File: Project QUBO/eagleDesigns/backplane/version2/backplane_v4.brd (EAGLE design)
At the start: 102 x 152 mm, 288 parts, among them U1 TUSB2077ALQFP

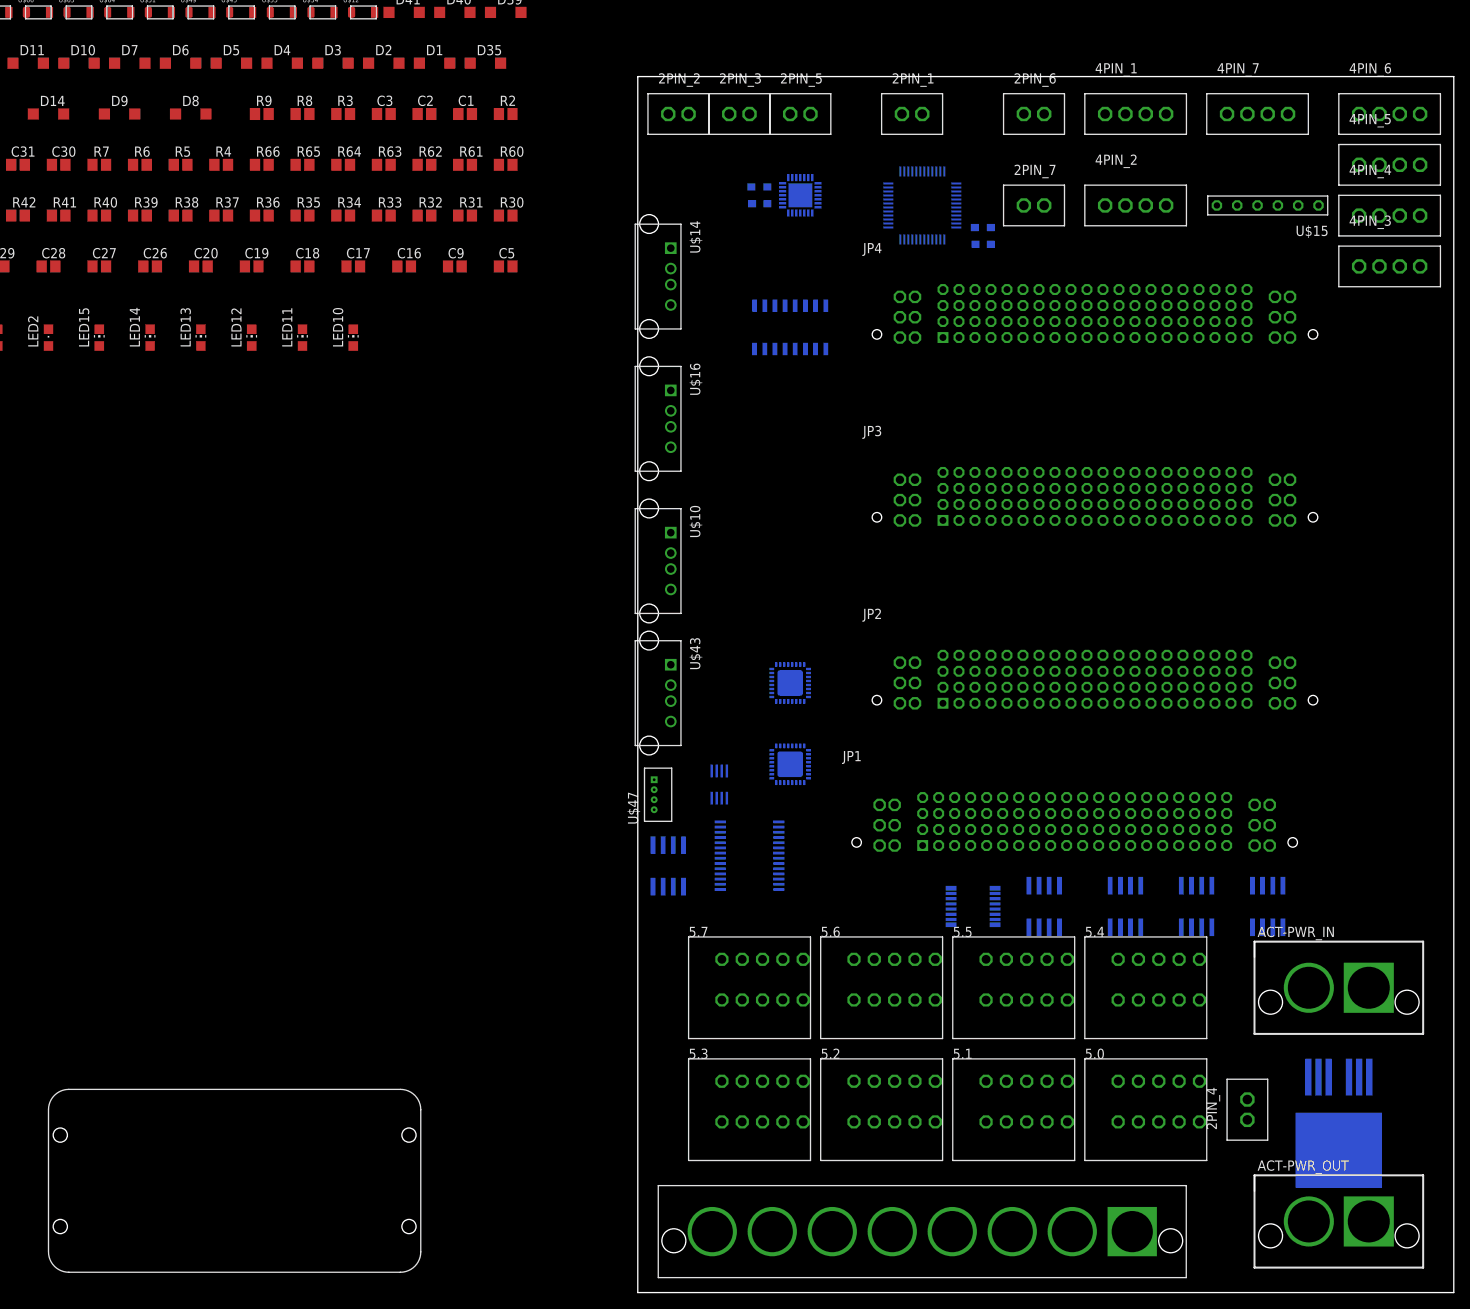
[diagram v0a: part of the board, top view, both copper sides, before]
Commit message: 
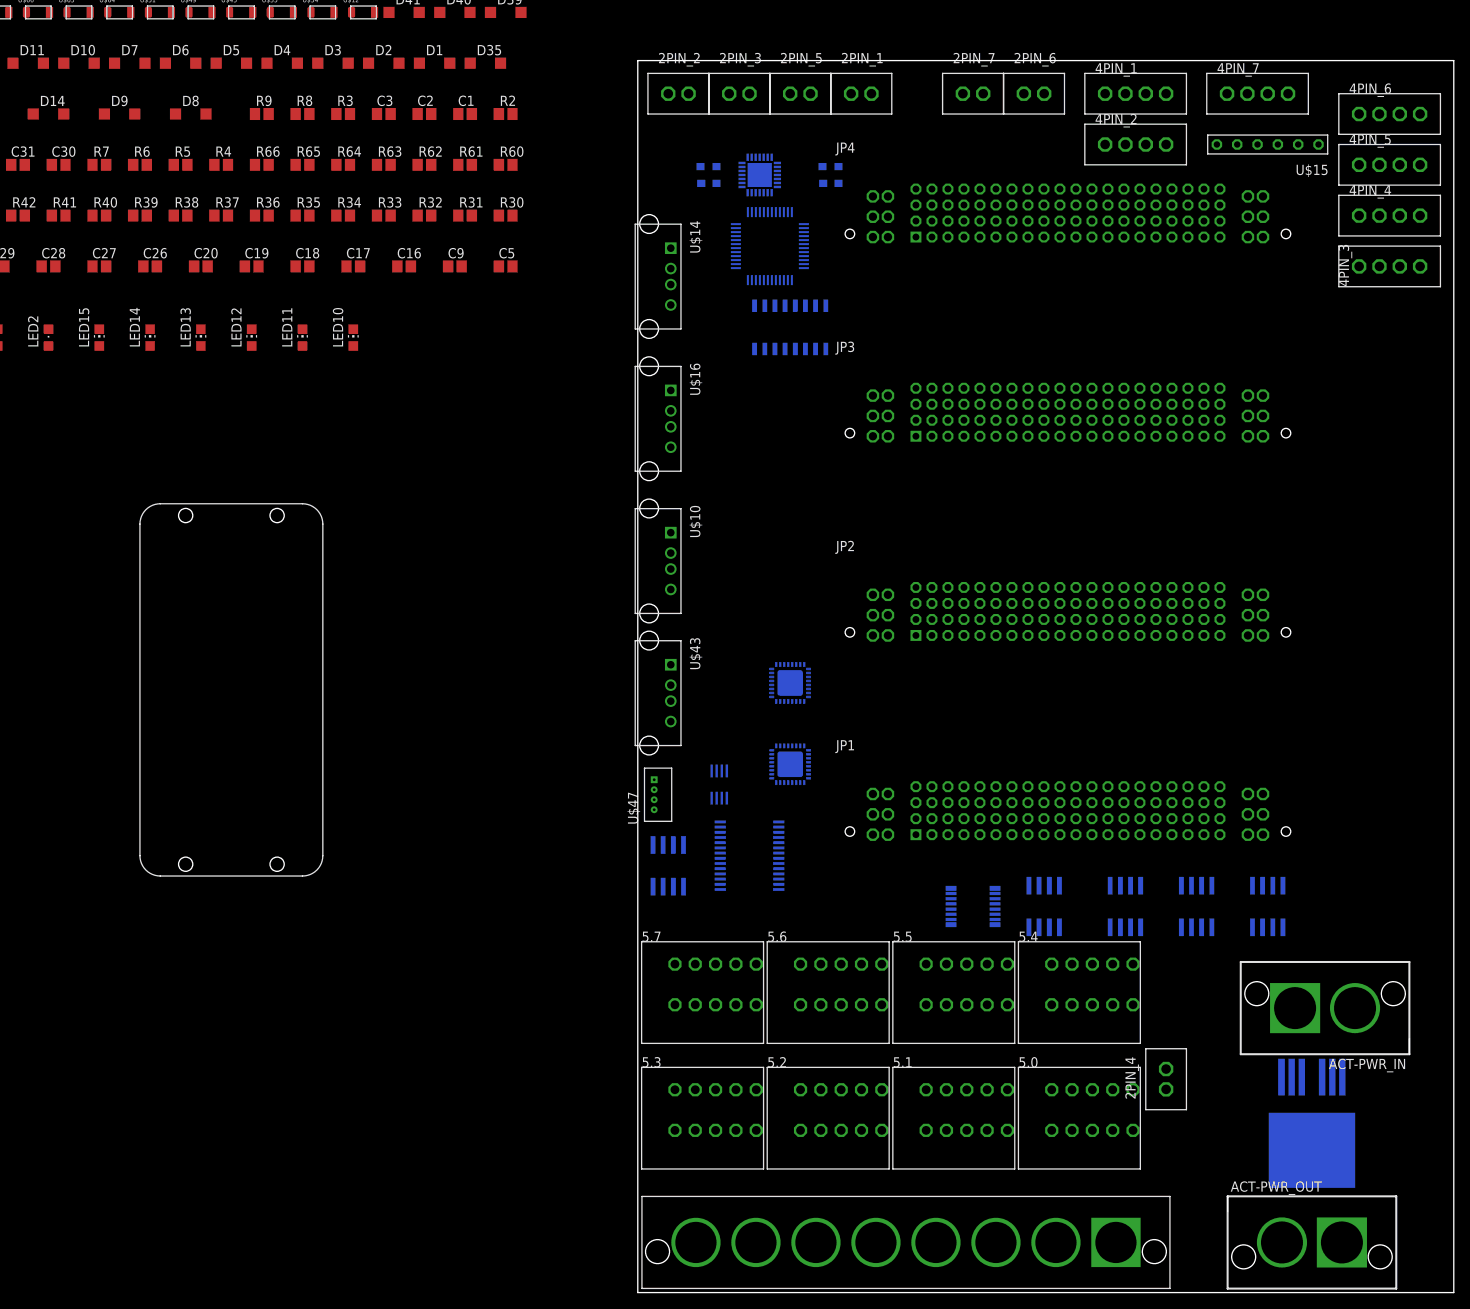
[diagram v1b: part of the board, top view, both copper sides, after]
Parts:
- moved U$13 60.2 mm to (-39.4, 52.1), turned to 90 degrees
- moved U$33 20.5 mm to (24.1, 139.7)
- moved U1 19.7 mm to (16.5, 130.8)
- moved 2PIN_7 15.9 mm to (41.9, 149.9)
- moved JP4 13.0 mm to (53.8, 134.5)
- moved JP3 11.0 mm to (53.8, 109.6)
- moved 2PIN_4 10.9 mm to (66.0, 26.7)
- moved JP2 9.13 mm to (53.8, 84.7)
- moved 5.0 8.37 mm to (55.2, 21.8)
- moved 5.4 8.32 mm to (55.2, 37.5)
- moved 4PIN_2 7.62 mm to (62.2, 143.5)
- moved U$15 7.62 mm to (78.7, 143.5)
- moved 5.1 7.56 mm to (39.5, 21.8)
- moved 5.5 7.51 mm to (39.5, 37.5)
- moved 2PIN_1 6.84 mm to (27.9, 149.9)
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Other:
- board size 102 x 152 mm -> 102 x 154 mm

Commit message: 
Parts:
- moved 5.4 35.1 mm to (23.8, 21.8)
- moved 5.3 35.1 mm to (39.5, 37.5)
- moved 5.1 22.2 mm to (55.2, 37.5)
- moved 5.6 22.2 mm to (8.10, 21.8)
- moved 5.2 15.7 mm to (39.5, 21.8)
- moved 5.5 15.7 mm to (23.8, 37.5)
- moved U$100 6.35 mm to (39.9, 6.26)
- moved ACT-PWR_OUT 5.08 mm to (84.3, 11.3)
- moved ACT-PWR_IN 4.02 mm to (84.6, 39.4)
- moved U$41 3.81 mm to (84.3, 21.6)
- moved 2PIN_3 2.54 mm to (15.2, 149.9)
- moved 2PIN_2 2.54 mm to (7.62, 149.9)
- moved 2PIN_1 2.54 mm to (30.5, 149.9)
- moved 2PIN_5 2.54 mm to (22.9, 149.9)
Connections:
- net 5V: now also U$10.VDD, U$43.VDD; no longer U$10.1, U$43.1
- net AHRS_USB_M: now also U$43.D+; no longer U$43.3
- net AHRS_USB_P: now also U$43.D-; no longer U$43.2
- net GND: now also U$10.GND, U$14.GND, U$16.GND, U$43.GND; no longer U$10.4, U$14.4, U$16.4, U$43.4
- net IMU_USB_M: now also U$10.D+; no longer U$10.3
- net IMU_USB_P: now also U$10.D-; no longer U$10.2
- net USB_5_5V: now also U$14.VDD; no longer U$14.1
- net USB_5_M: now also U$14.D+; no longer U$14.3
- net USB_5_P: now also U$14.D-; no longer U$14.2
- net USB_6_5V: now also U$16.VDD; no longer U$16.1
- net USB_6_M: now also U$16.D+; no longer U$16.3
- net USB_6_P: now also U$16.D-; no longer U$16.2

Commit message: 
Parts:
- added U$101, U$102, U$103, U$104, U$105, U$106, U$107, U$108, U$109, U$17, U$21, U$26, U$36, U$74: (no value), resistor:R0805
- moved U$14 1.27 mm to (2.54, 128.3)
- moved U$10 1.27 mm to (2.54, 92.7)
- moved U$16 1.27 mm to (2.54, 110.5)
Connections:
- removed net GND1: D37.A, U$11.P$1, U$12.P$2
- removed net GND2: D36.A, U$44.P$1, U$45.P$2
- removed net GND3: D10.A, U$48.P$1, U$49.P$2
- removed net USB_5_5V1: D37.C, U$11.P$2, U$12.P$1
- removed net USB_5_5V2: D36.C, U$44.P$2, U$45.P$1
- removed net USB_5_5V3: D10.C, U$48.P$2, U$49.P$1
- new net N$27: U$10.VDD, U$17.2
- new net N$28: U$10.GND, U$21.2
- new net N$29: U$10.SHIELD, U$10.SHIELD1, U$26.2
- new net N$30: U$108.2, U$47.P$1
- new net N$37: U$109.2, U$47.P$4
- new net N$38: U$43.VDD, U$74.2
- new net N$40: U$101.2, U$43.GND
- new net N$41: U$36.2, U$43.SHIELD, U$43.SHIELD1
- new net N$42: U$107.2, U$14.VDD
- new net N$73: U$106.2, U$14.GND
- new net N$80: U$105.2, U$14.SHIELD, U$14.SHIELD1
- new net N$83: U$104.2, U$16.SHIELD, U$16.SHIELD1
- new net N$84: U$102.2, U$16.VDD
- new net N$85: U$103.2, U$16.GND
- net 5V: now also D10.C, D36.C, D37.C, U$108.1, U$11.P$2, U$12.P$1, U$17.1, U$44.P$2, U$45.P$1, U$48.P$2, U$49.P$1, U$74.1; no longer U$10.VDD, U$43.VDD, U$47.P$1
- net GND: now also D10.A, D36.A, D37.A, U$101.1, U$103.1, U$104.1, U$105.1, U$106.1, U$109.1, U$11.P$1, U$12.P$2, U$21.1, U$26.1, U$36.1, U$44.P$1, U$45.P$2, U$48.P$1, U$49.P$2; no longer U$10.GND, U$14.GND, U$16.GND, U$43.GND, U$47.P$4
- net USB_5_5V: now also U$107.1; no longer U$14.VDD
- net USB_6_5V: now also U$102.1; no longer U$16.VDD

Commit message: 
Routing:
- added copper zone on layer 16, net ACT-PWR_POST-KILL
- added copper zone on layer 16, net ACT-PWR_PRE-KILL

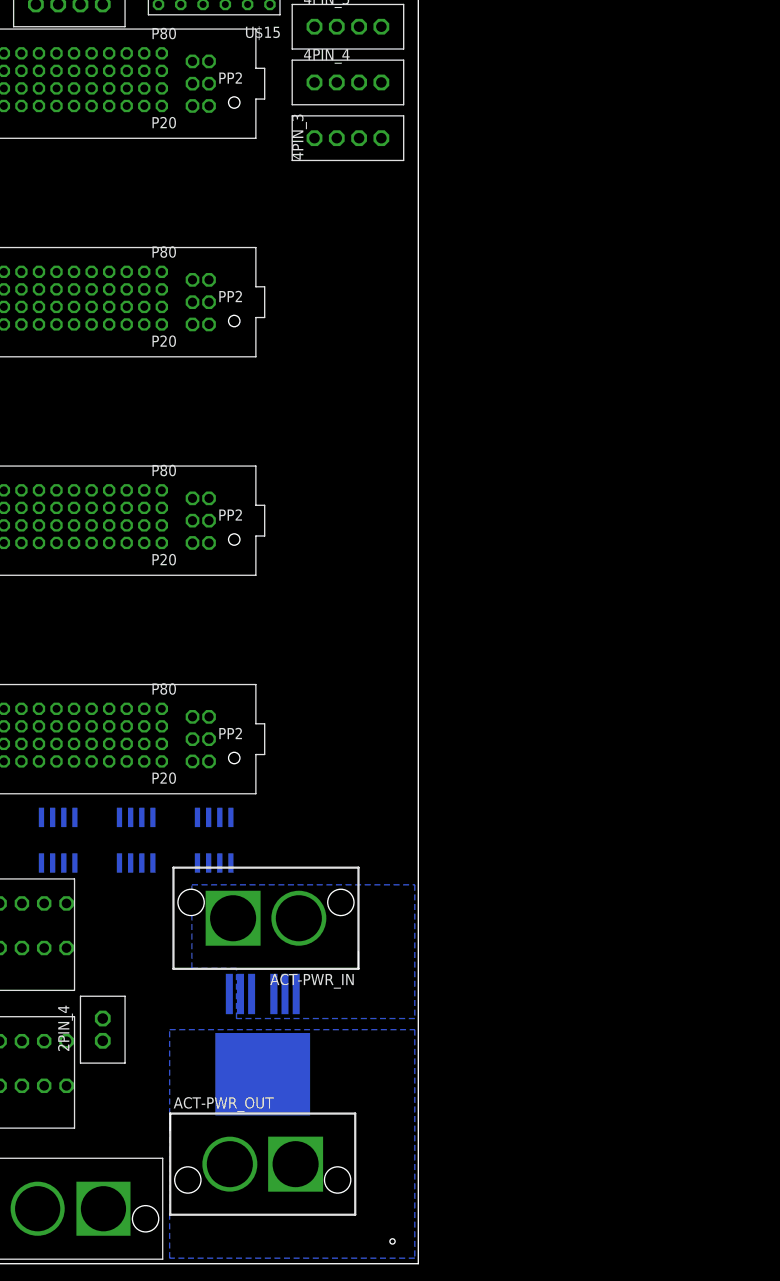
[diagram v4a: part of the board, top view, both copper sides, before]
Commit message: 
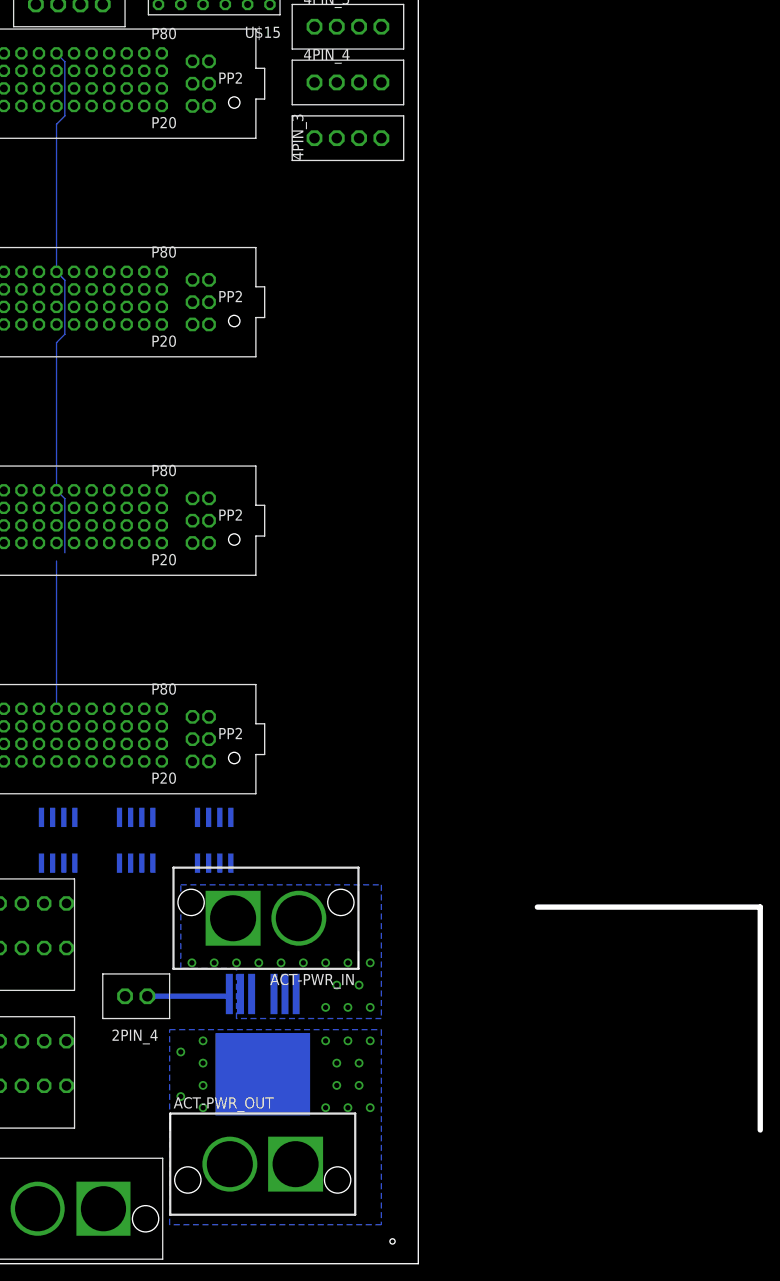
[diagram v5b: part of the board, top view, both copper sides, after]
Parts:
- moved 2PIN_4 5.39 mm to (69.8, 30.5), turned to 180 degrees
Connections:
- net RTS_0 renamed RX_SF
- net SCL_0_UNBUF renamed BATT_SCL_UNBUF
- net SDA_0_UNBUF renamed BATT_SDA_UNBUF
- removed net CTS_0: JP1.47, JP2.47, JP3.47, JP4.47
- removed net CTS_1: JP1.31, JP2.31, JP3.31, JP4.31
- removed net CTS_2: 4PIN_1.P$1, JP1.71, JP2.71, JP3.71, JP4.71
- removed net CTS_3: 4PIN_2.P$1, JP1.75, JP2.75, JP3.75, JP4.75
- removed net CTS_4: JP1.79, JP2.79, JP3.79, JP4.79
- removed net CTS_5: 5.2.P$5, 5.2.P$6, JP1.67, JP2.67, JP3.67, JP4.67, U$55.P$3
- removed net GND\: DVL_USB_HUB.P$29, JP1.40, JP2.40, JP3.40, JP4.40
- removed net GPIO_0: JP1.35, JP2.35, JP3.35, JP4.35
- removed net GPIO_1: JP1.38, JP2.38, JP3.38, JP4.38
- removed net GPIO_3: JP1.57, JP2.57, JP3.57, JP4.57
- removed net GPIO_4: JP1.58, JP2.58, JP3.58, JP4.58
- removed net NC: JP1.13, JP1.14, JP1.16, JP1.17, JP2.13, JP2.14, JP2.16, JP2.17, JP3.13, JP3.14, JP3.16, JP3.17, JP4.13, JP4.14, JP4.16, JP4.17
- removed net RTS_1: JP1.32, JP2.32, JP3.32, JP4.32
- removed net RTS_2: 4PIN_1.P$2, JP1.72, JP2.72, JP3.72, JP4.72
- removed net RTS_3: 4PIN_2.P$2, JP1.76, JP2.76, JP3.76, JP4.76
- removed net RTS_4: JP1.80, JP2.80, JP3.80, JP4.80
- removed net RTS_5: 5.2.P$7, 5.2.P$8, JP1.68, JP2.68, JP3.68, JP4.68, U$55.P$2
- removed net RX_0: JP1.45, JP2.45, JP3.45, JP4.45
- removed net RX_1: JP1.29, JP2.29, JP3.29, JP4.29
- removed net RX_2: 4PIN_1.P$4, JP1.69, JP2.69, JP3.69, JP4.69, U$4.P$3
- removed net RX_3: 4PIN_2.P$4, JP1.73, JP2.73, JP3.73, JP4.73, U$8.P$2
- removed net RX_4: JP1.77, JP2.77, JP3.77, JP4.77
- removed net RX_5: 5.2.P$1, 5.2.P$2, JP1.65, JP2.65, JP3.65, JP4.65, U$54.P$2
- removed net SCL_0: JP1.28, JP2.28, JP3.28, JP4.28, U$38.2
- removed net SCL_1: 2PIN_6.P$1, JP1.10, JP2.10, JP3.10, JP4.10, U$18.P$2, U$50.2
- removed net SCL_2: 5.4.P$10, 5.4.P$9, JP1.60, JP2.60, JP3.60, JP4.60, U$63.P$2
- removed net SCL_3: 5.3.P$3, 5.3.P$4, JP1.6, JP2.6, JP3.6, JP4.6, U$52.P$2
- removed net SDA_0: JP1.27, JP2.27, JP3.27, JP4.27, U$38.7
- removed net SDA_1: 2PIN_6.P$2, JP1.9, JP2.9, JP3.9, JP4.9, U$18.P$3, U$50.7
- removed net SDA_2: 5.5.P$10, 5.5.P$9, JP1.59, JP2.59, JP3.59, JP4.59, U$63.P$3
- removed net SDA_3: 5.3.P$1, 5.3.P$2, JP1.5, JP2.5, JP3.5, JP4.5, U$52.P$3
- removed net TX_0: JP1.46, JP2.46, JP3.46, JP4.46
- removed net TX_1: JP1.30, JP2.30, JP3.30, JP4.30
- removed net TX_2: 4PIN_1.P$3, JP1.70, JP2.70, JP3.70, JP4.70, U$4.P$2
- removed net TX_3: 4PIN_2.P$3, JP1.74, JP2.74, JP3.74, JP4.74, U$8.P$3
- removed net TX_4: JP1.78, JP2.78, JP3.78, JP4.78
- removed net TX_5: 5.2.P$3, 5.2.P$4, JP1.66, JP2.66, JP3.66, JP4.66, U$54.P$3
- removed net USB_1_M: JP1.19, R2.1, R22.1, U$29.P$3
- removed net USB_2_M: JP2.19, R24.1, R37.1, U$30.P$3
- removed net USB_3_M: JP3.19, R27.2, R40.1, U$31.P$3
- removed net USB_4_M: JP4.19, R28.2, R41.1, U$32.P$3
- new net ACT_SCL: 5.4.P$10, 5.4.P$9, JP1.24, JP2.24, JP3.24, JP4.24, U$63.P$2
- new net ACT_SDA: 5.5.P$10, 5.5.P$9, JP1.23, JP2.23, JP3.23, JP4.23, U$63.P$3
- new net BATT_SCL: JP1.44, JP2.44, JP3.44, JP4.44, U$38.2
- new net BATT_SDA: JP1.43, JP2.43, JP3.43, JP4.43, U$38.7
- new net CTS_CF: 4PIN_2.P$1, JP1.13, JP2.13, JP3.13, JP4.13
- new net CTS_MC: 4PIN_1.P$1, JP1.29, JP2.29, JP3.29, JP4.29
- new net CTS_MD: 5.2.P$5, 5.2.P$6, JP1.68, JP2.68, JP3.68, JP4.68, U$55.P$3
- new net CTS_MF: JP1.5, JP2.5, JP3.5, JP4.5
- new net CTS_PF: JP1.9, JP2.9, JP3.9, JP4.9
- new net CTS_SF: JP1.50, JP2.50, JP3.50, JP4.50
- new net EXT_SCL: 5.3.P$3, 5.3.P$4, JP1.34, JP2.34, JP3.34, JP4.34, U$52.P$2
- new net EXT_SDA: 5.3.P$1, 5.3.P$2, JP1.33, JP2.33, JP3.33, JP4.33, U$52.P$3
- new net GPIO_22: JP1.22, JP2.22, JP3.22, JP4.22
- new net GPIO_63: JP1.63, JP2.63, JP3.63, JP4.63
- new net INT_SCL: 2PIN_6.P$1, JP1.65, JP2.65, JP3.65, JP4.65, U$18.P$2, U$50.2
- new net INT_SDA: 2PIN_6.P$2, JP1.64, JP2.64, JP3.64, JP4.64, U$18.P$3, U$50.7
- new net RTS_CF: 4PIN_2.P$2, JP1.14, JP2.14, JP3.14, JP4.14
- new net RTS_MC: 4PIN_1.P$2, JP1.30, JP2.30, JP3.30, JP4.30
- new net RTS_MD: 5.2.P$7, 5.2.P$8, JP1.69, JP2.69, JP3.69, JP4.69, U$55.P$2
- new net RTS_MF: JP1.6, JP2.6, JP3.6, JP4.6
- new net RTS_PF: JP1.10, JP2.10, JP3.10, JP4.10
- new net RTS_SF: JP1.51, JP2.51, JP3.51, JP4.51
- new net RX_CF: 4PIN_2.P$4, JP1.11, JP2.11, JP3.11, JP4.11, U$8.P$2
- new net RX_MC: 4PIN_1.P$4, JP1.27, JP2.27, JP3.27, JP4.27, U$4.P$3
- new net RX_MD: 5.2.P$1, 5.2.P$2, JP1.66, JP2.66, JP3.66, JP4.66, U$54.P$2
- new net RX_MF: JP1.3, JP2.3, JP3.3, JP4.3
- new net RX_PF: JP1.7, JP2.7, JP3.7, JP4.7
- new net TX_CF: 4PIN_2.P$3, JP1.12, JP2.12, JP3.12, JP4.12, U$8.P$3
- new net TX_MC: 4PIN_1.P$3, JP1.28, JP2.28, JP3.28, JP4.28, U$4.P$2
- new net TX_MD: 5.2.P$3, 5.2.P$4, JP1.67, JP2.67, JP3.67, JP4.67, U$54.P$3
- new net TX_MF: JP1.4, JP2.4, JP3.4, JP4.4
- new net TX_PF: JP1.8, JP2.8, JP3.8, JP4.8
- new net TX_SF: JP1.49, JP2.49, JP3.49, JP4.49
- new net USB_1_N: JP1.61, R2.1, R22.1, U$29.P$3
- new net USB_2_N: JP2.61, R24.1, R37.1, U$30.P$3
- new net USB_3_N: JP3.61, R27.2, R40.1, U$31.P$3
- new net USB_4_N: JP4.61, R28.2, R41.1, U$32.P$3
- net 12V: now also JP1.16, JP1.36, JP1.56, JP1.76, JP2.16, JP2.36, JP2.56, JP2.76, JP3.16, JP3.36, JP3.56, JP3.76, JP4.16, JP4.36, JP4.56, JP4.76; no longer JP1.1, JP1.21, JP1.41, JP1.61, JP2.1, JP2.21, JP2.41, JP2.61, JP3.1, JP3.21, JP3.41, JP3.61, JP4.1, JP4.21, JP4.41, JP4.61
- net 3V3: now also JP1.18, JP1.38, JP1.58, JP1.78, JP2.18, JP2.38, JP2.58, JP2.78, JP3.18, JP3.38, JP3.58, JP3.78, JP4.18, JP4.38, JP4.58, JP4.78; no longer JP1.23, JP1.3, JP1.43, JP1.63, JP2.23, JP2.3, JP2.43, JP2.63, JP3.23, JP3.3, JP3.43, JP3.63, JP4.23, JP4.3, JP4.43, JP4.63
- net 5V: now also JP1.17, JP1.37, JP1.57, JP1.77, JP2.17, JP2.37, JP2.57, JP2.77, JP3.17, JP3.37, JP3.57, JP3.77, JP4.17, JP4.37, JP4.57, JP4.77; no longer JP1.2, JP1.22, JP1.42, JP1.62, JP2.2, JP2.22, JP2.42, JP2.62, JP3.2, JP3.22, JP3.42, JP3.62, JP4.2, JP4.22, JP4.42, JP4.62
- net CANH: now also JP1.45, JP2.45, JP3.45, JP4.45; no longer JP1.25, JP2.25, JP3.25, JP4.25
- net CANL: now also JP1.46, JP2.46, JP3.46, JP4.46; no longer JP1.26, JP2.26, JP3.26, JP4.26
- net CE_2: now also JP1.52, JP2.52, JP3.52, JP4.52; no longer JP1.54, JP2.54, JP3.54, JP4.54
- net CE_3: now also JP1.53, JP2.53, JP3.53, JP4.53; no longer JP1.55, JP2.55, JP3.55, JP4.55
- net CE_4: now also JP1.54, JP2.54, JP3.54, JP4.54; no longer JP1.56, JP2.56, JP3.56, JP4.56
- net CE_CPU: now also JP1.74, JP2.74, JP3.74, JP4.74; no longer JP1.53, JP2.53, JP3.53, JP4.53
- net CE_LEDS: now also JP1.73, JP2.73, JP3.73, JP4.73; no longer JP1.52, JP2.52, JP3.52, JP4.52
- net GND: now also DVL_USB_HUB.P$29, JP1.1, JP1.19, JP1.20, JP1.21, JP1.25, JP1.32, JP1.35, JP1.40, JP1.42, JP1.47, JP1.55, JP1.59, JP1.60, JP1.62, JP1.75, JP1.79, JP1.80, JP1.P1,1, JP1.P1,2, JP1.P1,3, JP1.P1,4, JP1.P1,5, JP1.P1,6, JP2.1, JP2.19, JP2.20, JP2.21, JP2.25, JP2.32, JP2.35, JP2.40, JP2.42, JP2.47, JP2.55, JP2.59, JP2.60, JP2.62, JP2.75, JP2.79, JP2.80, JP2.P1,1, JP2.P1,2, JP2.P1,3, JP2.P1,4, JP2.P1,5, JP2.P1,6, JP3.1, JP3.19, JP3.20, JP3.21, JP3.25, JP3.32, JP3.35, JP3.40, JP3.42, JP3.47, JP3.55, JP3.59, JP3.60, JP3.62, JP3.75, JP3.79, JP3.80, JP3.P1,1, JP3.P1,2, JP3.P1,3, JP3.P1,4, JP3.P1,5, JP3.P1,6, JP4.1, JP4.19, JP4.20, JP4.21, JP4.25, JP4.32, JP4.35, JP4.40, JP4.42, JP4.47, JP4.55, JP4.59, JP4.60, JP4.62, JP4.75, JP4.79, JP4.80, JP4.P1,1, JP4.P1,2, JP4.P1,3, JP4.P1,4, JP4.P1,5, JP4.P1,6; no longer JP1.12, JP1.18, JP1.24, JP1.33, JP1.34, JP1.36, JP1.37, JP1.4, JP1.44, JP1.64, JP1.P2,1, JP1.P2,2, JP1.P2,3, JP1.P2,4, JP1.P2,5, JP1.P2,6, JP2.12, JP2.18, JP2.24, JP2.33, JP2.34, JP2.36, JP2.37, JP2.4, JP2.44, JP2.64, JP2.P2,1, JP2.P2,2, JP2.P2,3, JP2.P2,4, JP2.P2,5, JP2.P2,6, JP3.12, JP3.18, JP3.24, JP3.33, JP3.34, JP3.36, JP3.37, JP3.4, JP3.44, JP3.64, JP3.P2,1, JP3.P2,2, JP3.P2,3, JP3.P2,4, JP3.P2,5, JP3.P2,6, JP4.12, JP4.18, JP4.24, JP4.33, JP4.34, JP4.36, JP4.37, JP4.4, JP4.44, JP4.64, JP4.P2,1, JP4.P2,2, JP4.P2,3, JP4.P2,4, JP4.P2,5, JP4.P2,6
- net GPIO_2: now also JP1.2, JP2.2, JP3.2, JP4.2; no longer JP1.11, JP2.11, JP3.11, JP4.11
- net MISO: now also JP1.72, JP2.72, JP3.72, JP4.72; no longer JP1.51, JP2.51, JP3.51, JP4.51
- net MOSI: now also JP1.71, JP2.71, JP3.71, JP4.71; no longer JP1.50, JP2.50, JP3.50, JP4.50
- net PWM_0: now also JP1.31, JP2.31, JP3.31, JP4.31; no longer JP1.7, JP2.7, JP3.7, JP4.7
- net PWM_1: now also JP1.26, JP2.26, JP3.26, JP4.26; no longer JP1.8, JP2.8, JP3.8, JP4.8
- net SPI_CLK: now also JP1.70, JP2.70, JP3.70, JP4.70; no longer JP1.49, JP2.49, JP3.49, JP4.49
- net USB_1_P: now also JP1.41; no longer JP1.20
- net USB_2_P: now also JP2.41; no longer JP2.20
- net USB_3_P: now also JP3.41; no longer JP3.20
- net USB_4_P: now also JP4.41; no longer JP4.20
- net V_BATT: now also JP1.P2,1, JP1.P2,2, JP1.P2,3, JP1.P2,4, JP1.P2,5, JP1.P2,6, JP2.P2,1, JP2.P2,2, JP2.P2,3, JP2.P2,4, JP2.P2,5, JP2.P2,6, JP3.P2,1, JP3.P2,2, JP3.P2,3, JP3.P2,4, JP3.P2,5, JP3.P2,6, JP4.P2,1, JP4.P2,2, JP4.P2,3, JP4.P2,4, JP4.P2,5, JP4.P2,6; no longer JP1.P1,1, JP1.P1,2, JP1.P1,3, JP1.P1,4, JP1.P1,5, JP1.P1,6, JP2.P1,1, JP2.P1,2, JP2.P1,3, JP2.P1,4, JP2.P1,5, JP2.P1,6, JP3.P1,1, JP3.P1,2, JP3.P1,3, JP3.P1,4, JP3.P1,5, JP3.P1,6, JP4.P1,1, JP4.P1,2, JP4.P1,3, JP4.P1,4, JP4.P1,5, JP4.P1,6
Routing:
- net 5V: track 0.00 -> 80.7 mm
- net 3V3: track 0.00 -> 80.7 mm
- net 12V: track 0.00 -> 80.7 mm
- net CE_CPU: track 0.00 -> 75.7 mm
- net KILL-SWT-GATE: track 0.00 -> 9.60 mm
- net TX_MD: track 0.00 -> 5.08 mm
- net SHORE_SCL: track 0.00 -> 5.08 mm
- net RX_MD: track 0.00 -> 5.08 mm
- net RTS_MD: track 0.00 -> 5.08 mm
- net DVL_STX: track 0.00 -> 5.08 mm
- net DVL_SRX: track 0.00 -> 5.08 mm
- net DVL_HTX: track 0.00 -> 5.08 mm
- net DVL_HRX: track 0.00 -> 5.08 mm
- net DVL_HRTS: track 0.00 -> 5.08 mm
- net DVL_HCTS: track 0.00 -> 5.08 mm
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- added copper zone on layer 15, net ACT-PWR_POST-KILL
- added copper zone on layer 15, net ACT-PWR_PRE-KILL
- added copper zone on layer 2, net GND
- added copper zone on layer 15, net V_BATT
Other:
- board size 102 x 154 mm -> 141 x 154 mm

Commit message: 
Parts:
- added R67, R68, R72: 1.5k, resistor:R0805
- moved U$47 78.1 mm to (68.2, 20.0), turned to 0 degrees
- moved U$14 16.2 mm to (9.23, 113.5), turned to 0 degrees
- moved U$43 12.3 mm to (9.57, 85.0), turned to 0 degrees
- moved DVL_HOST_FTDI 10.1 mm to (10.1, 71.7)
- moved U1 9.69 mm to (6.89, 129.6), turned to 270 degrees
- moved U$16 9.16 mm to (9.51, 104.5), turned to 0 degrees
- moved DVL_SLAVE_FTDI 8.14 mm to (25.1, 71.5)
- moved U$10 7.32 mm to (9.29, 95.5), turned to 0 degrees
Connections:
- net AHRS_USB_M renamed AHRS_USB_N
- net DVL_USB_M renamed DVL_USB_N
- net EXT_USB_M renamed EXT_USB_N
- net HUB_USB_M renamed HUB_USB_N
- net IMU_USB_M renamed IMU_USB_N
- removed net N$52: DVL_USB_HUB.P$23
- net 3V3: now also R67.2, R68.2, R72.2
- net HUB_USB_P: now also R72.1
- net N$27: now also R67.1
- net N$38: now also R68.1
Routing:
- net CE_CPU: track 75.7 -> 4.04 mm
